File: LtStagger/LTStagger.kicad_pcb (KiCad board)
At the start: 2 copper layers, 151.4 x 105.6 mm, 51 parts, among them K0 K00, K1 K01, K10 K10, K11 K11, K12 K12, K2 K02, K20 K20, K21 K21, K22 K22, K30 K30, K31 K31, K32 K32, K33 K33, K40 K40, K41 K41, K42 K42, K43 K43, K50 K50, K51 K51, K53 K53, SW1 Rotary_Encoder_Switch, U1 ProMicro, U2 TRRS, U3 MCP23018-E_SP

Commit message: Maybe ready for production
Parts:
- added ?: , Digi:Right, B.Cu at (203.3, 101.4)
- added ?: , Digi:Left, F.Cu at (203.3, 101.4)
- moved U2 25.3 mm to (215.4, 81.7)
- moved R4 25.3 mm to (208.2, 88.8)
- moved R5 25.3 mm to (208.2, 74.3)
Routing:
- net Col5: track 129.7 -> 207.3 mm
- net SDA: track 147.3 -> 158.1 mm
- net SCL: track 145.7 -> 156.3 mm
- net VCC: track 167.3 -> 176.8 mm
- net GND: track 193.4 -> 198.1 mm
- net Col0: track 160.5 -> 163.1 mm
- net Col4: track 190.1 -> 191.6 mm
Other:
- outline, holes or cut-outs redrawn

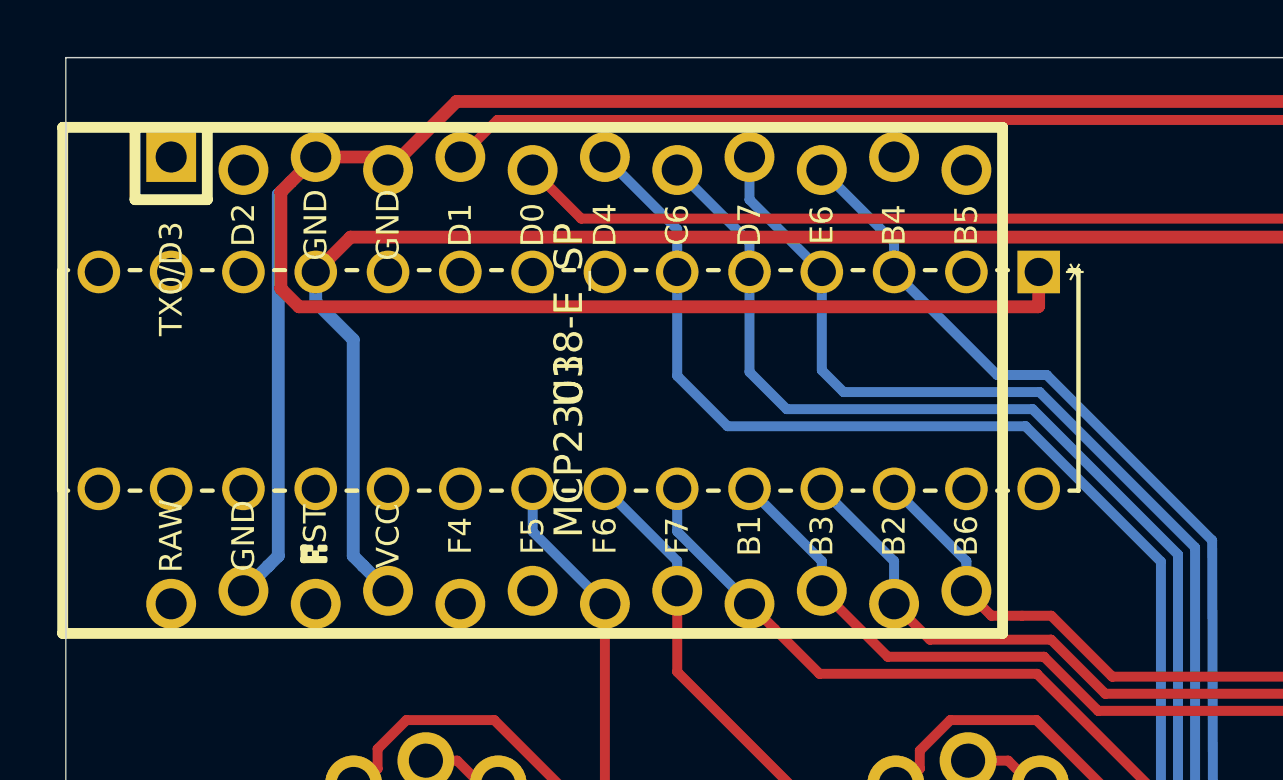
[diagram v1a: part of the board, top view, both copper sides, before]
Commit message: LTStagger 2, but that joystick is a bad idea
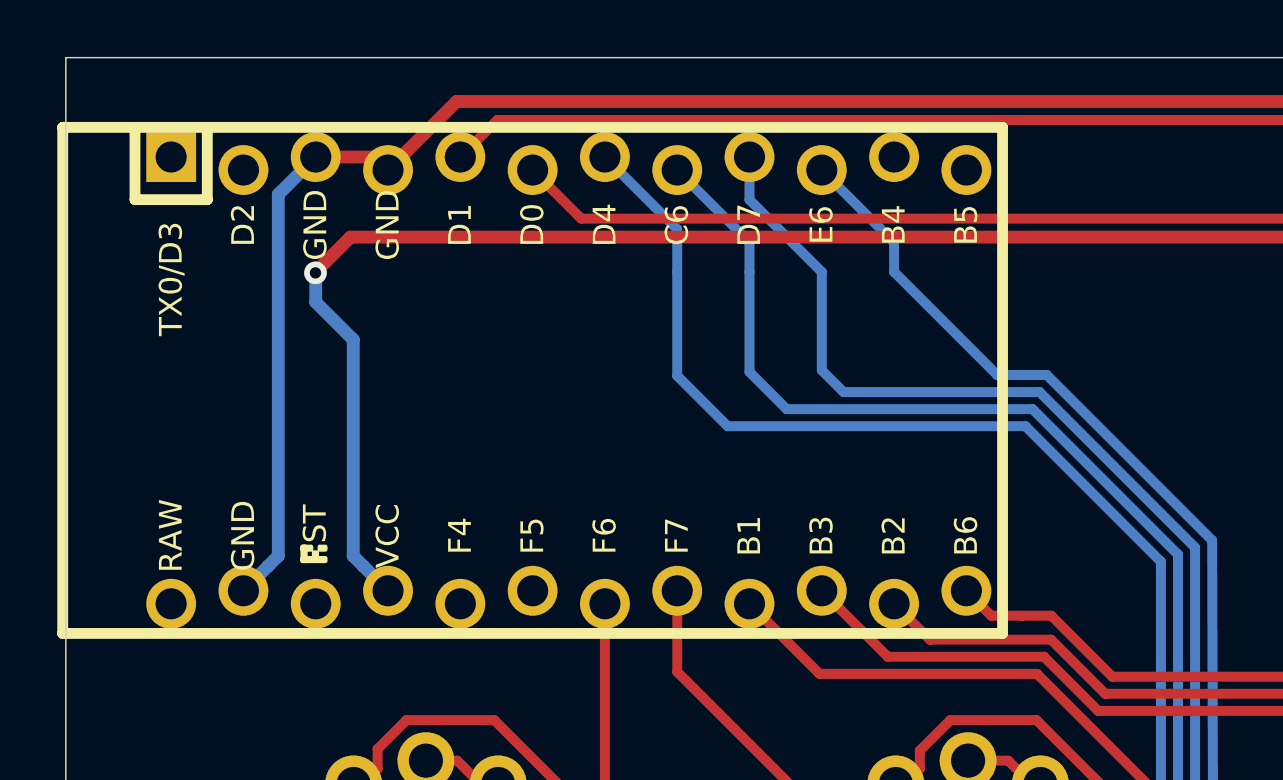
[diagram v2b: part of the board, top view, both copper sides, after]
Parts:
- removed U3: MCP23018-E_SP, Digi:MCP23018
- U1: footprint Keebio-Parts:ArduinoProMicro-ZigZag -> Digi:ArduinoProMicro-ZigZag
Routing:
- net GND: track 198.1 -> 164.9 mm
- net Col4: track 191.6 -> 186.5 mm
- net Col2: track 171.8 -> 166.7 mm
- net Col0: track 163.1 -> 158.0 mm
- net Col1: track 143.4 -> 138.8 mm
- net Col5: track 207.3 -> 202.7 mm
- net Col3: track 190.4 -> 185.8 mm
- net VCC: vias 0 -> 1
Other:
- net class Default removed
- net class Power removed
